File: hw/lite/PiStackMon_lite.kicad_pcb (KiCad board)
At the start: 2 copper layers, 59.7 x 18.8 mm, 31 parts, among them J1 Conn_01x03, J2 Conn_01x03, J3 5.08mm, J5 CUI PJ-102, P1 Conn_02x20_Odd_Even, U1 STP16CP05TTR

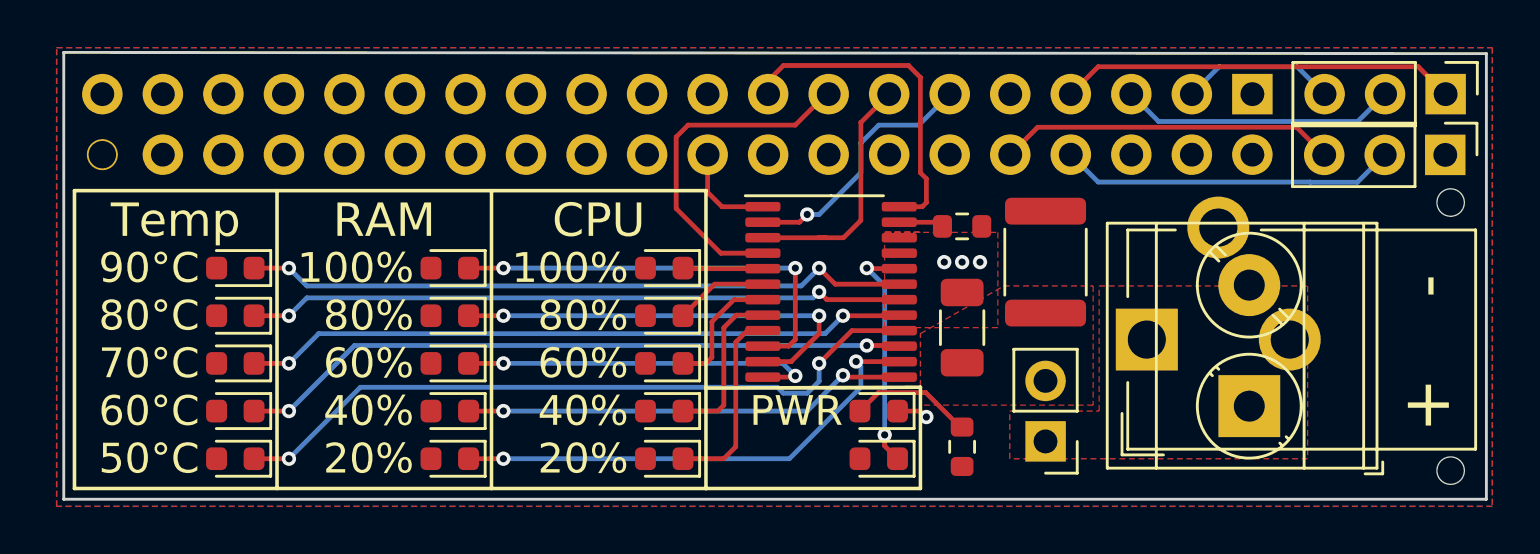
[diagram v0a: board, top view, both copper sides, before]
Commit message: Updating LED driver to TLC59282
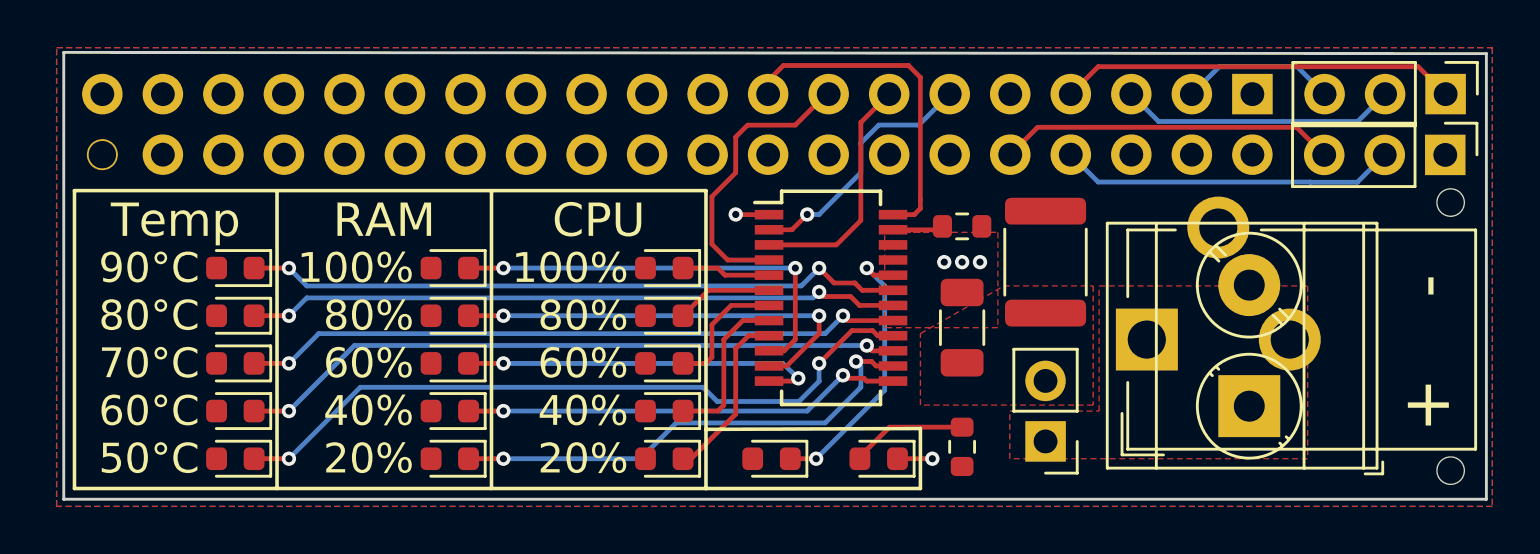
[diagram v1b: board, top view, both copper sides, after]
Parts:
- R2: value 7k5 -> 10k
- U1: value STP16CP05TTR -> TLC59282DBQR; footprint Package_SO:TSSOP-24_4.4x7.8mm_P0.65mm -> Package_SO:SSOP-24_3.9x8.7mm_P0.635mm
- moved D17 4.50 mm to (52.8, 45.5)
- moved D16 2.00 mm to (57.2, 45.5)
- moved U1 0.25 mm to (55.2, 38.8)
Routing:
- net GND: track 5.46 -> 2.87 mm, vias 4 -> 5
- net /GPIO22(GEN3): track 14.6 -> 12.2 mm
- net Net-(D17-Pad1): track 9.91 -> 11.9 mm
- net Net-(D1-Pad1): track 8.15 -> 7.36 mm
- net Net-(R2-Pad1): track 1.88 -> 2.46 mm
- net Net-(D5-Pad1): track 3.36 -> 3.88 mm

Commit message: Minor changes based on @bablokb's feedback
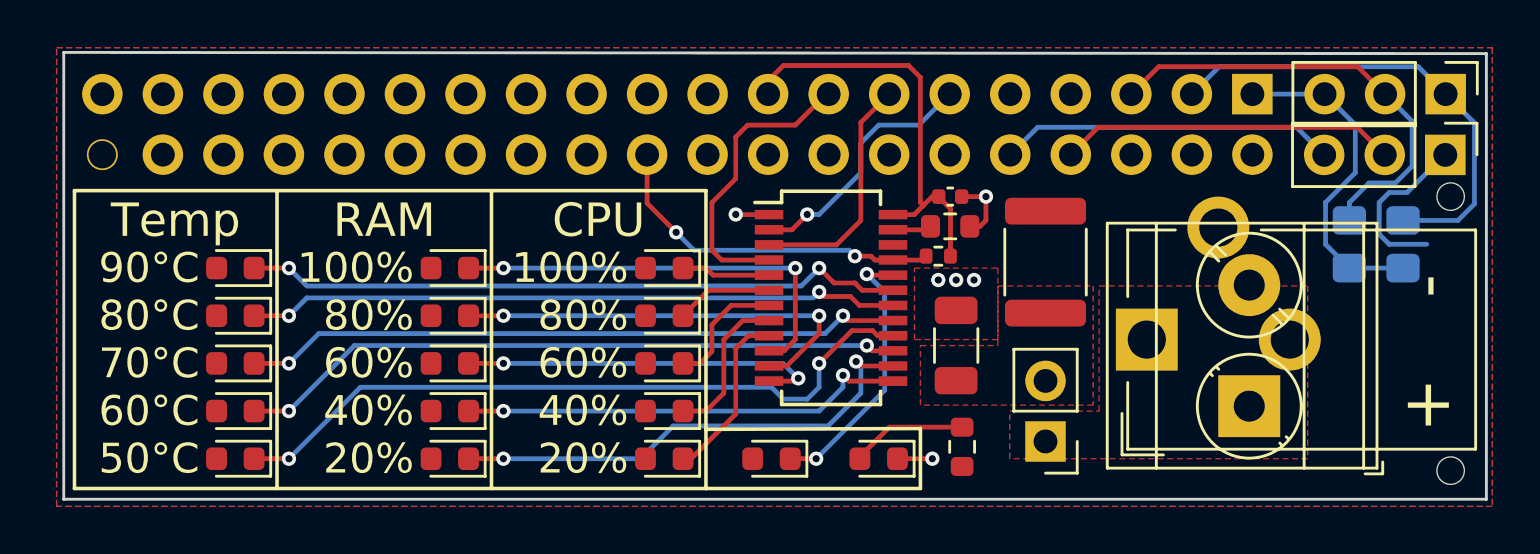
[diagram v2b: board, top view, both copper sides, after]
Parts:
- added C2: 100n, Capacitor_SMD:C_0402_1005Metric, F.Cu at (60.2, 34.5)
- added R1: NM, Resistor_SMD:R_0805_2012Metric_Pad1.20x1.40mm_HandSolder, B.Cu at (77.0, 36.5)
- added R4: NM, Resistor_SMD:R_0805_2012Metric_Pad1.20x1.40mm_HandSolder, B.Cu at (79.2, 36.5)
- added R5: 3k3, Resistor_SMD:R_0402_1005Metric, F.Cu at (59.8, 37.0)
- R3: value 1k -> 560R
- moved LOGO1 1.68 mm to (78.5, 42.0)
- moved C1 0.79 mm to (60.5, 40.8)
- moved R2 0.50 mm to (60.2, 35.8)
- moved H2 0.25 mm to (81.2, 34.5)
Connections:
- J1 pad 1: /GPIO4(1Wire_Default) -> /GPIO2(SDA1)
- J1 pad 3: /GPIO2(SDA1) -> /3V3_2
- U1 pad 21: GND -> /GPIO25(GEN6)
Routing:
- net /GPIO4(1Wire_Default): track 16.7 -> 0.00 mm
- net /GPIO25(GEN6): track 0.00 -> 14.8 mm, vias 0 -> 2
- net /3V3_2: track 0.00 -> 14.0 mm
- net /GPIO2(SDA1): track 6.52 -> 20.0 mm
- net GND: track 2.87 -> 12.8 mm, vias 5 -> 6
- net /GPIO3(SCL1): track 11.6 -> 19.1 mm
- net +3V3: track 14.2 -> 17.8 mm
- net Net-(R2-Pad1): track 2.46 -> 1.63 mm
